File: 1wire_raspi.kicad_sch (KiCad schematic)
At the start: 6 parts, among them J1 GPIO, J2 Power, J3 1Wire, J4 1Wire

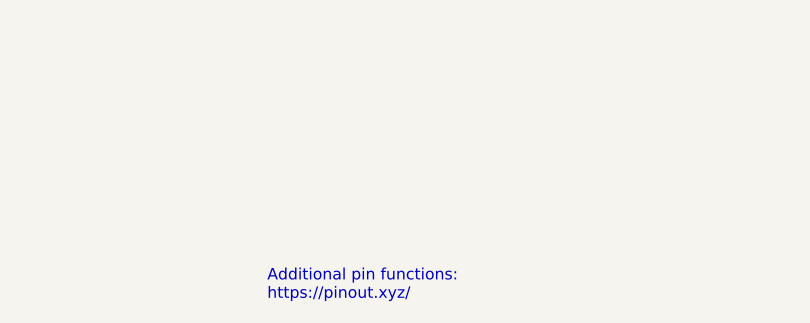
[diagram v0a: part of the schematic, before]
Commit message: Corrected page size
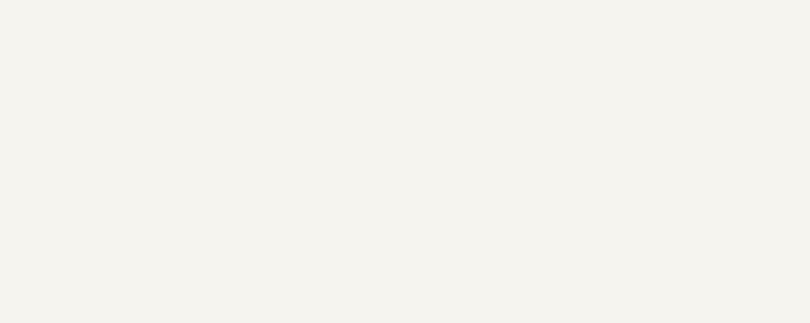
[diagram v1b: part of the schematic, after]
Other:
- note removed: "Additional pin functions: https://pinout.xyz/"
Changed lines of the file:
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@@
 		(company "Guy Corbaz")
 	)
-	(text "Additional pin functions:\nhttps://pinout.xyz/"
+	(text " "
 		(exclude_from_sim no)
 		(at 179.07 180.34 0)
